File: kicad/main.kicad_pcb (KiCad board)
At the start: 2 copper layers, 97.8 x 88.9 mm, 48 parts, among them J1 Jack-DC, J2 LCD, J3 Bus, J4 PWR, J5 uSD, J6 VIA_B, J7 IO~{EN}_{[2..7]}, J8 Control, P1 Mini-DIN-6, SW1 Step, SW2 Reset, X1 4 MHz

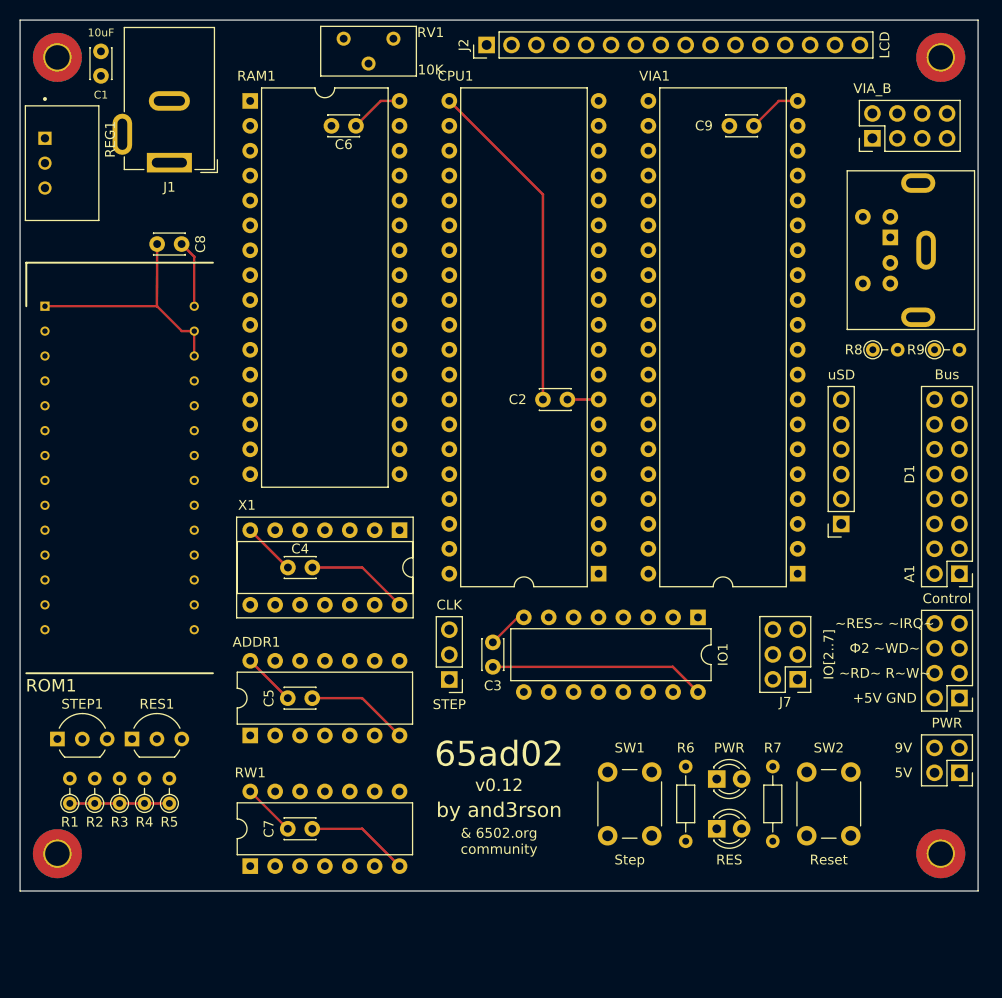
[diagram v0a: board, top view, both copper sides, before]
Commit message: V13 - 32K RAM + 24K ROM
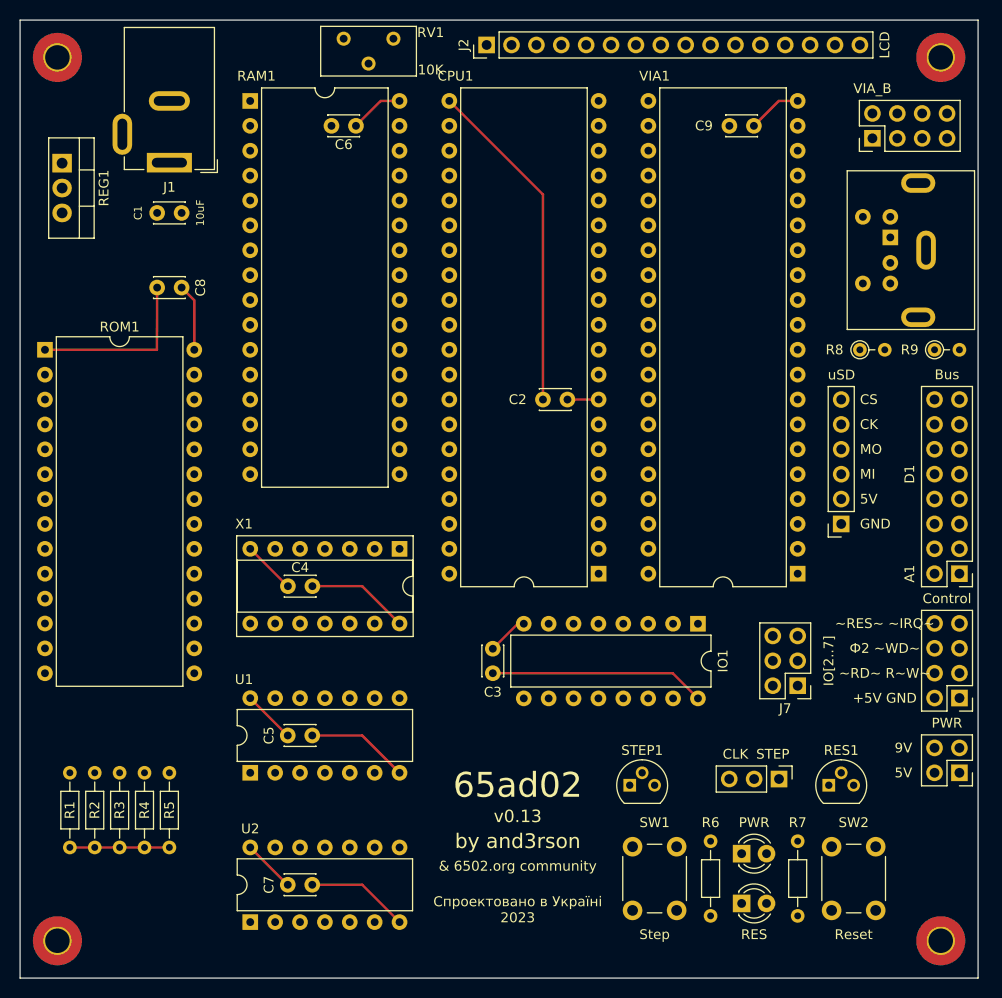
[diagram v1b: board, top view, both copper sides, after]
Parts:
- removed ADDR1: 74HC00, Package_DIP:DIP-14_W7.62mm
- added U1: 74HC00, Package_DIP:DIP-14_W7.62mm, F.Cu at (43.2, 94.0)
- R1, R2, R3, R4, R5: footprint Resistor_THT:R_Axial_DIN0204_L3.6mm_D1.6mm_P2.54mm_Vertical -> Resistor_THT:R_Axial_DIN0204_L3.6mm_D1.6mm_P7.62mm_Horizontal
- REG1: footprint footprints:CONV_TSR_1-2450 -> Package_TO_SOT_THT:TO-220-3_Vertical
- RES1, STEP1: footprint Package_TO_SOT_THT:TO-92_Inline_Wide -> Package_TO_SOT_THT:TO-92
- ROM1: footprint 28-526-10:DIPS1524W61P254L4191H673Q28N -> Package_DIP:DIP-28_W15.24mm
- moved RES1 71.3 mm to (102.2, 95.2)
- moved STEP1 58.6 mm to (81.9, 95.2)
- moved JP1 35.2 mm to (97.2, 94.6), turned to -90 degrees
- moved C1 18.4 mm to (36.2, 36.8), turned to 180 degrees
- moved REF** 8.89 mm to (23.5, 111.1)
- moved REF** 8.89 mm to (113.7, 111.1)
- moved D1 8.03 mm to (93.3, 102.2)
- moved D2 8.03 mm to (93.3, 107.3)
- moved R7 8.03 mm to (99.1, 101.0)
- moved SW2 8.03 mm to (102.5, 108.0)
- moved SW1 8.03 mm to (82.2, 108.0)
- moved R6 8.03 mm to (90.2, 108.6)
- moved C7 5.72 mm to (47.0, 105.4)
- moved U2 5.72 mm to (43.2, 109.2)
- moved R1 4.49 mm to (24.8, 101.6)
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- renumbered RW1 to U2
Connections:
- R7 pad 2: Net-(D2-A) -> Net-(R7-Pad2)
- RAM1 pad 22: RAM~{EN} -> A_{15}
- RAM1 pad 31: A_{15} -> +5V
- ROM1 pad 26: GND -> A_{13}
- ROM1 pad 27: GND -> A_{14}
- U2 pad 11: unconnected-(RW1-Pad11) -> Net-(D2-A)
- U2 pad 12: unconnected-(RW1-Pad12) -> Net-(R7-Pad2)
- U2 pad 13: unconnected-(RW1-Pad13) -> Net-(R7-Pad2)
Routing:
- net GND: track 90.2 -> 82.8 mm
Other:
- board size 97.8 x 88.9 mm -> 97.8 x 97.8 mm
- board text added: "v0.13"
- board text added: "Спроектовано в Україні 2023"
- board text removed: "v0.12"

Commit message: WIP: v0.14
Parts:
- ROM1: footprint Package_DIP:DIP-28_W15.24mm -> 28-526-10:DIPS1524W61P254L4191H673Q28N
- moved R1 55.3 mm to (80.0, 103.5), turned to 180 degrees
- moved R2 52.7 mm to (80.0, 101.0), turned to 180 degrees
- moved R3 50.3 mm to (80.0, 98.4), turned to 180 degrees
- moved R4 48.0 mm to (80.0, 95.9), turned to 180 degrees
- moved R5 45.8 mm to (80.0, 93.3), turned to 180 degrees
- moved C5 21.4 mm to (26.0, 94.6), turned to -90 degrees
- moved U1 21.2 mm to (22.2, 90.8), turned to 0 degrees
- moved U2 20.2 mm to (34.9, 90.8), turned to 0 degrees
- moved C7 13.6 mm to (38.7, 94.6), turned to -90 degrees
- moved STEP1 3.81 mm to (85.7, 95.2)
- moved C4 2.54 mm to (47.0, 77.5)
- moved X1 2.54 mm to (58.4, 73.7)
- moved JP1 1.28 mm to (98.4, 94.6)
- moved RES1 1.28 mm to (103.5, 95.2)
- moved SW1 1.28 mm to (83.5, 108.0)
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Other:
- board text added: "v0.14"
- board text added: "Спроектовано в Україні, 2023"
- board text removed: "v0.13"
- board text removed: "Спроектовано в Україні 2023"

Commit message: WIP: v0.15
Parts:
- removed REF** (x4): MountingHole_2.5mm_Pad_TopBottom, MountingHole:MountingHole_2.5mm_Pad_TopBottom
- added ACIA1: W65C51N6TPG, Package_DIP:DIP-28_W15.24mm_Socket, F.Cu at (71.1, 53.3)
- added C10: 0.1uF, Capacitor_THT:C_Disc_D3.0mm_W2.0mm_P2.50mm, F.Cu at (30.5, 48.3)
- added C11: 0,1uF, Capacitor_THT:C_Disc_D3.0mm_W2.0mm_P2.50mm, F.Cu at (52.1, 80.0)
- added C12: 10uF, Capacitor_THT:CP_Radial_D5.0mm_P2.50mm, F.Cu at (71.2, 35.6)
- added C13: 10uF, Capacitor_THT:CP_Radial_D5.0mm_P2.50mm, F.Cu at (71.2, 45.7)
- added C14: 10uF, Capacitor_THT:CP_Radial_D5.0mm_P2.50mm, F.Cu at (63.5, 45.7)
- added C15: 10uF, Capacitor_THT:CP_Radial_D5.0mm_P2.50mm, F.Cu at (63.5, 35.6)
- added C16: 0.1uF, Capacitor_THT:C_Disc_D3.0mm_W2.0mm_P2.50mm, F.Cu at (63.5, 58.4)
- added J10: RS232, Connector_Dsub:DSUB-9_Male_Horizontal_P2.77x2.84mm_EdgePinOffset4.94mm_Housed_MountingHolesOffset7.48mm, F.Cu at (56.4, 25.8)
- added J9: Addr, Connector_PinHeader_2.54mm:PinHeader_1x08_P2.54mm_Vertical, F.Cu at (139.7, 91.4)
- added JP2: ACIA~{IRQ}, Connector_PinHeader_2.54mm:PinHeader_1x02_P2.54mm_Vertical, F.Cu at (68.6, 83.8)
- added JP3: ACIA~{NMI}, Connector_PinHeader_2.54mm:PinHeader_1x02_P2.54mm_Vertical, F.Cu at (68.6, 76.2)
- added JP4: VIA~{IRQ}, Connector_PinHeader_2.54mm:PinHeader_1x02_P2.54mm_Vertical, F.Cu at (167.6, 76.2)
- added JP5: VIA~{NMI}, Connector_PinHeader_2.54mm:PinHeader_1x02_P2.54mm_Vertical, F.Cu at (175.3, 76.2)
- added MH1: MountingHole, my:Hole_3.5x5, F.Cu at (23.8, 111.4)
- added MH2: MountingHole, my:Hole_3.5x5, F.Cu at (206.8, 111.5)
- added U3: MAX232, Package_DIP:DIP-16_W7.62mm_Socket, F.Cu at (55.9, 38.1)
- added X2: 1.8432 MHz, Package_DIP:DIP-14_W7.62mm_Socket, F.Cu at (58.4, 76.2)
- CPU1, VIA1: footprint Package_DIP:DIP-40_W15.24mm -> Package_DIP:DIP-40_W15.24mm_Socket
- IO1: footprint Package_DIP:DIP-16_W7.62mm -> Package_DIP:DIP-16_W7.62mm_Socket
- J2: value LCD -> LCD_Conn; footprint Connector_PinHeader_2.54mm:PinHeader_1x16_P2.54mm_Vertical -> my:LCD_4004
- J3: value Bus -> Data; footprint Connector_PinHeader_2.54mm:PinHeader_2x08_P2.54mm_Vertical -> Connector_PinHeader_2.54mm:PinHeader_1x08_P2.54mm_Vertical
- J5: footprint Connector_PinSocket_2.54mm:PinSocket_1x06_P2.54mm_Vertical -> my:MicroSD-Adapter
- J6, J8: footprint Connector_PinHeader_2.54mm:PinHeader_2x04_P2.54mm_Vertical -> Connector_PinHeader_2.54mm:PinHeader_1x08_P2.54mm_Vertical
- J7: footprint Connector_PinHeader_2.54mm:PinHeader_2x03_P2.54mm_Vertical -> Connector_PinHeader_2.54mm:PinHeader_1x06_P2.54mm_Vertical
- RAM1: footprint Package_DIP:DIP-32_W15.24mm -> Package_DIP:DIP-32_W15.24mm_Socket
- ROM1: footprint 28-526-10:DIPS1524W61P254L4191H673Q28N -> Socket:DIP_Socket-28_W11.9_W12.7_W15.24_W17.78_W18.5_3M_228-1277-00-0602J
- U1, U2: footprint Package_DIP:DIP-14_W7.62mm -> Package_DIP:DIP-14_W7.62mm_Socket
- moved C3 124.8 mm to (191.1, 61.0), turned to 90 degrees
- moved P1 103.2 mm to (201.6, 83.8)
- moved R8 95.6 mm to (193.0, 88.9), turned to 90 degrees
- moved J4 93.0 mm to (208.3, 101.6)
- moved SW2 89.5 mm to (193.3, 107.4)
- moved R7 87.9 mm to (188.2, 100.9)
- moved C5 87.1 mm to (113.0, 97.8)
- moved U1 87.1 mm to (109.2, 94.0)
- moved C7 87.1 mm to (125.7, 97.8)
- moved U2 87.1 mm to (121.9, 94.0)
- moved D1 86.0 mm to (180.6, 100.9)
- moved D2 86.0 mm to (180.6, 107.8)
- moved R9 85.6 mm to (193.0, 81.3), turned to -90 degrees
- moved C8 84.2 mm to (96.1, 101.0), turned to -90 degrees
- moved R6 84.1 mm to (175.6, 108.5)
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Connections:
- net Net-(CPU1-~{NMI}) renamed ~{NMI}
- IO1 pad 14: unconnected-(IO1-O1-Pad14) -> ACIA~{EN}
- J2 pad 1: GND -> unconnected-(J2-Pin_1-Pad1)
- J2 pad 10: unconnected-(J2-Pin_10-Pad10) -> LCDR~{W}
- J2 pad 11: PA_{0} -> LCDRS
- J2 pad 12: PA_{1} -> Net-(J2-Pin_12)
- J2 pad 13: PA_{2} -> GND
- J2 pad 14: PA_{3} -> +5V
- J2 pad 15: +5V -> LCDEN2
- J2 pad 16: GND -> unconnected-(J2-Pin_16-Pad16)
- J2 pad 2: +5V -> unconnected-(J2-Pin_2-Pad2)
- J2 pad 3: Net-(J2-Pin_3) -> unconnected-(J2-Pin_3-Pad3)
- J2 pad 4: PA_{6} -> unconnected-(J2-Pin_4-Pad4)
- J2 pad 5: PA_{5} -> LCDD4
- J2 pad 6: PA_{4} -> LCDD5
- J2 pad 7: unconnected-(J2-Pin_7-Pad7) -> LCDD6
- J2 pad 8: unconnected-(J2-Pin_8-Pad8) -> LCDD7
- J2 pad 9: unconnected-(J2-Pin_9-Pad9) -> LCDEN1
- J3 pad 1: A_{0} -> D_{0}
- J3 pad 2: A_{1} -> D_{1}
- J3 pad 3: A_{2} -> D_{2}
- J3 pad 4: A_{3} -> D_{3}
- J3 pad 5: A_{4} -> D_{4}
- J3 pad 6: A_{5} -> D_{5}
- J3 pad 7: A_{6} -> D_{6}
- J3 pad 8: A_{7} -> D_{7}
- J6 pad 7: Net-(J6-Pin_7) -> +5V
- J6 pad 8: Net-(J6-Pin_8) -> GND
- P1 pad 1: PA_{7} -> PS2DATA
- P1 pad 5: CA1 -> PS2CLK
- R8 pad 1: CA1 -> PS2CLK
- R9 pad 1: PA_{7} -> PS2DATA
- RV1 pad 2: Net-(J2-Pin_3) -> Net-(J2-Pin_12)
- VIA1 pad 14: Net-(J6-Pin_3) -> PS2DATA
- VIA1 pad 15: Net-(J6-Pin_4) -> Net-(J6-Pin_3)
- VIA1 pad 16: Net-(J6-Pin_5) -> Net-(J6-Pin_4)
- VIA1 pad 17: Net-(J6-Pin_6) -> Net-(J6-Pin_5)
- VIA1 pad 18: Net-(J6-Pin_7) -> PS2CLK
- VIA1 pad 19: Net-(J6-Pin_8) -> Net-(J6-Pin_6)
- VIA1 pad 2: PA_{0} -> LCDD4
- VIA1 pad 21: ~{IRQ} -> Net-(JP4-B)
- VIA1 pad 3: PA_{1} -> LCDD5
- VIA1 pad 4: PA_{2} -> LCDD6
- VIA1 pad 40: CA1 -> unconnected-(VIA1-CA1-Pad40)
- VIA1 pad 5: PA_{3} -> LCDD7
- VIA1 pad 6: PA_{4} -> LCDEN1
- VIA1 pad 7: PA_{5} -> LCDEN2
- VIA1 pad 8: PA_{6} -> LCDR~{W}
- VIA1 pad 9: PA_{7} -> LCDRS
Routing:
- net +5V: track 74.5 -> 113.3 mm
- net GND: track 82.8 -> 52.9 mm
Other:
- board size 97.8 x 97.8 mm -> 190.5 x 97.2 mm
- board text added: "ACIA~IRQ~"
- board text added: "ACIA~NMI~"
- board text added: "Addr"
- board text added: "Control"
- board text added: "Data"
- board text added: "IO~EN~[2..7]"
- board text added: "VIA_B"
- board text added: "VIA~IRQ~"
- board text added: "VIA~NMI~"
- board text added: "v0.15"
- board text removed: "v0.14"

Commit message: WIP: v0.15
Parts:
- removed C10: 0.1uF, Capacitor_THT:C_Disc_D3.0mm_W2.0mm_P2.50mm
- added JP6: ~, Connector_PinHeader_2.54mm:PinHeader_1x03_P2.54mm_Vertical, F.Cu at (33.0, 33.0)
- added JP7: ~, Connector_PinHeader_2.54mm:PinHeader_1x03_P2.54mm_Vertical, F.Cu at (33.0, 38.1)
- added JP8: ~, Connector_PinHeader_2.54mm:PinHeader_1x03_P2.54mm_Vertical, F.Cu at (33.0, 43.2)
- added JP9: ~, Connector_PinHeader_2.54mm:PinHeader_1x03_P2.54mm_Vertical, F.Cu at (33.0, 48.3)
- ROM1: footprint Socket:DIP_Socket-28_W11.9_W12.7_W15.24_W17.78_W18.5_3M_228-1277-00-0602J -> my:ZIF28
- moved U3 5.08 mm to (61.0, 38.1)
- moved C12 2.54 mm to (73.7, 35.6)
- moved C13 2.54 mm to (73.7, 45.7)
- moved C6 2.54 mm to (78.7, 25.4)
- moved C14 2.54 mm to (66.1, 45.7)
- moved C15 2.54 mm to (66.1, 35.6)
- moved RAM1 2.54 mm to (81.3, 25.4)
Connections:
- J2 pad 1: unconnected-(J2-Pin_1-Pad1) -> Net-(J2-Pin_1)
- J2 pad 2: unconnected-(J2-Pin_2-Pad2) -> Net-(J2-Pin_2)
- J2 pad 3: unconnected-(J2-Pin_3-Pad3) -> Net-(J2-Pin_3)
- J2 pad 4: unconnected-(J2-Pin_4-Pad4) -> Net-(J2-Pin_4)
- J2 pad 5: LCDD4 -> Net-(J2-Pin_5)
- J2 pad 6: LCDD5 -> Net-(J2-Pin_6)
- J2 pad 7: LCDD6 -> Net-(J2-Pin_7)
- J2 pad 8: LCDD7 -> Net-(J2-Pin_8)
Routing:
- net GND: track 52.9 -> 44.3 mm
- net +5V: track 113.3 -> 108.0 mm
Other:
- board text added: "v0.16"
- board text removed: "v0.15"

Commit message: v0.15
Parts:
- removed JP6, JP7, JP8, JP9: ~, Connector_PinHeader_2.54mm:PinHeader_1x03_P2.54mm_Vertical
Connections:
- J2 pad 1: Net-(J2-Pin_1) -> LCDD7
- J2 pad 2: Net-(J2-Pin_2) -> LCDD6
- J2 pad 3: Net-(J2-Pin_3) -> LCDD5
- J2 pad 4: Net-(J2-Pin_4) -> LCDD4
- J2 pad 5: Net-(J2-Pin_5) -> LCDD4
- J2 pad 6: Net-(J2-Pin_6) -> LCDD5
- J2 pad 7: Net-(J2-Pin_7) -> LCDD6
- J2 pad 8: Net-(J2-Pin_8) -> LCDD7
- U1 pad 10: A_{14} -> A_{15}
- U1 pad 13: A_{14} -> A_{15}
- VIA1 pad 18: PS2CLK -> Net-(J6-Pin_6)
- VIA1 pad 19: Net-(J6-Pin_6) -> PS2CLK
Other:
- board text added: "v0.15"
- board text removed: "v0.16"

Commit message: Snake!
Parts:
- added J11: UART, Connector_PinHeader_2.54mm:PinHeader_1x04_P2.54mm_Horizontal, F.Cu at (76.2, 20.3)
- added JP6: ~{CTS}, Connector_PinHeader_2.54mm:PinHeader_1x02_P2.54mm_Vertical, F.Cu at (35.6, 76.2)
- R6: value 5K -> 20K
- R7: value 5K -> 10K
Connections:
- net Net-(ACIA1-XTAL1) renamed ACIACLK
- R7 pad 1: ~{RES} -> Net-(R7-Pad1)
- R7 pad 2: Net-(R7-Pad2) -> Net-(D2-A)
- U2 pad 11: Net-(D2-A) -> Net-(R7-Pad1)
- U2 pad 12: Net-(R7-Pad2) -> ~{RES}
- U2 pad 13: Net-(R7-Pad2) -> ~{RES}
